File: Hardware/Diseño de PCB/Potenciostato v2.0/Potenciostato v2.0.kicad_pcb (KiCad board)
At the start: 2 copper layers, 82 x 100 mm, 129 parts, among them IC1 LMP7702MAX_NOPB, IC2 LMP7701MFX_NOPB, IC3 LMP7701MFX_NOPB, IC4 MAX5217GUA+, IC5 MAX4477ASA+, IC6 LM4040AIM3X-2.5_NOPB, IC7 LM4040A50IDBZR, IC8 OPA354AIDBVT, J1 Conn_Coaxial, J2 Conn_02x15_Odd_Even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

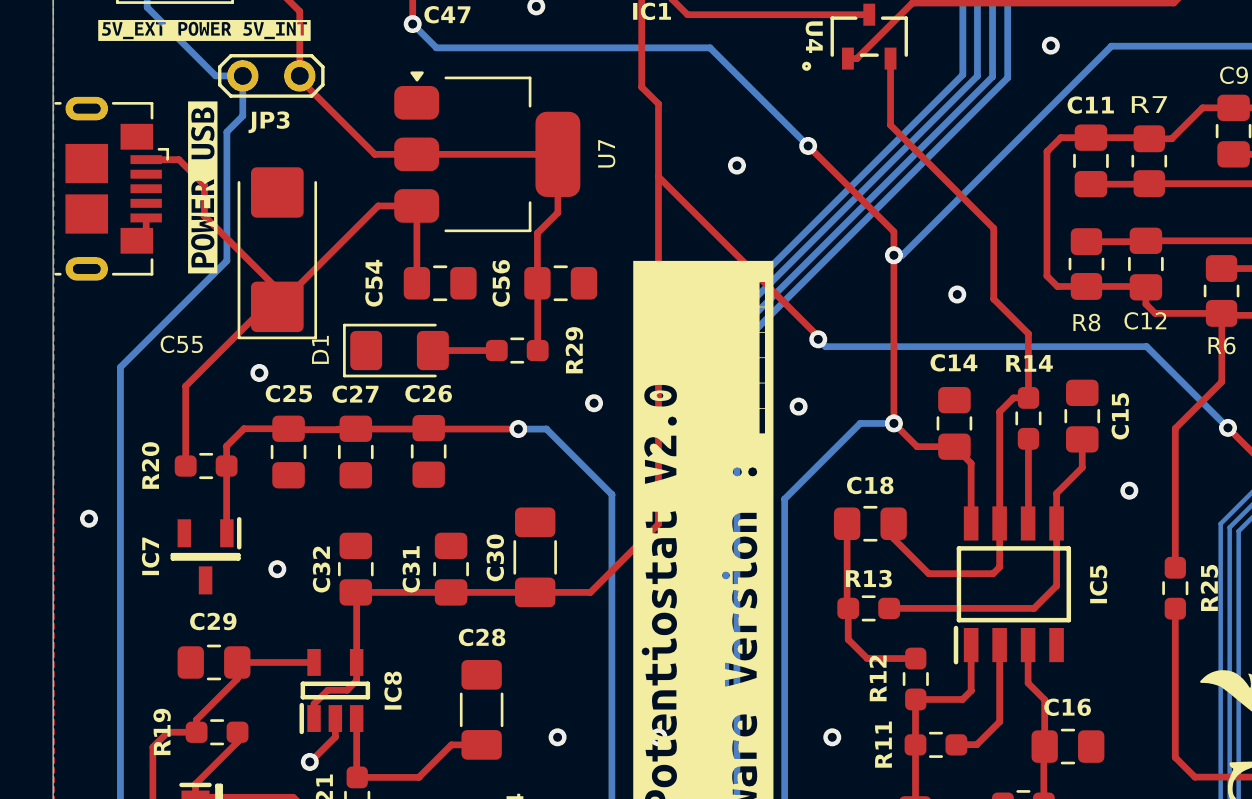
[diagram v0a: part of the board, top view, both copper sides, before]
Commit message: Hardware modifications. More notes added to the KiCad project related to hardware issues found during testing. USB Power and ground inverted corrected in design and PCB. MAX4477 replaced by OPA2320 in design and PCB. More notes with recommendations and advised can now be found in the schematics.
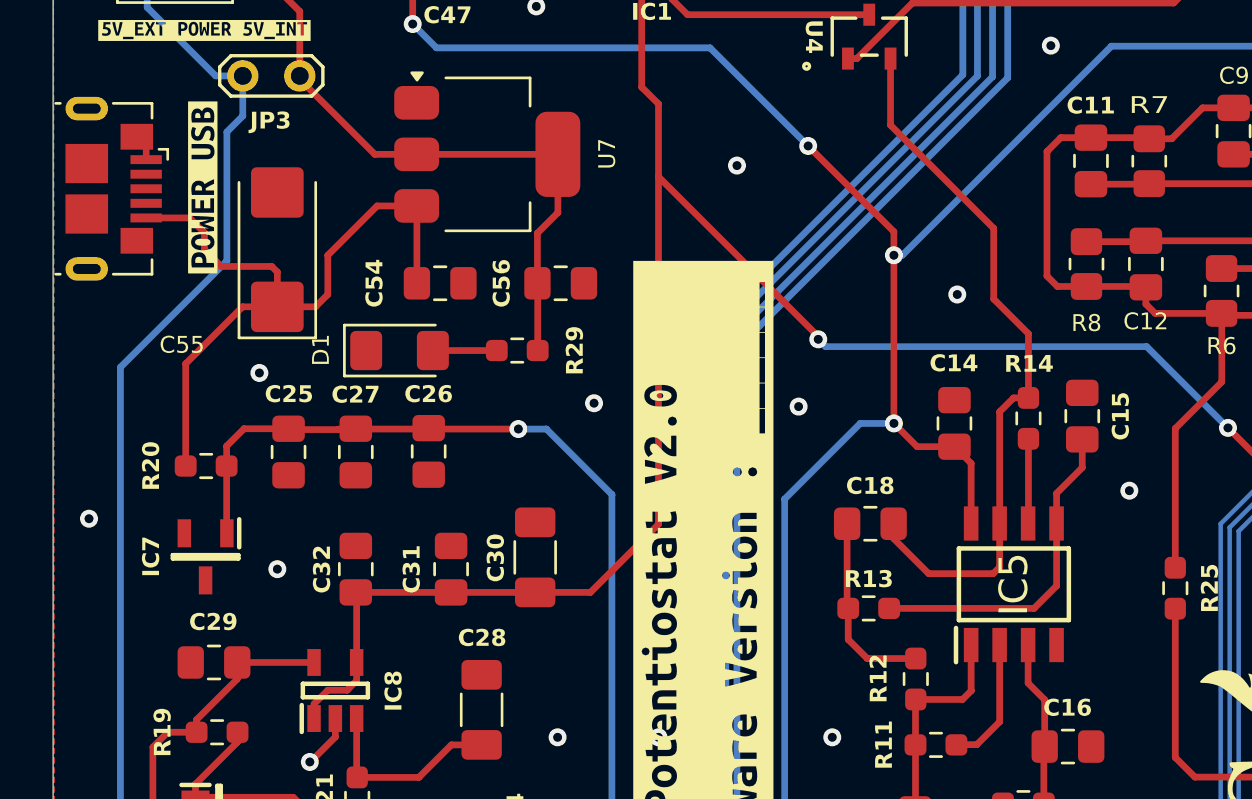
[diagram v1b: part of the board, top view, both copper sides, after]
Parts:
- C30: value 100u -> 10u
- C31: value 0.1u -> 1u
- C32: value 47u -> 0.1u
- IC5: value MAX4477ASA+ -> OPA2320AIDR; footprint potentiostat:SOIC127P600X175_MAX4477 -> potentiostat:SOIC127P600X175-8N
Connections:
- net /Etapa Amplificadora - Electrodos/X1 renamed /Amplifier Stage - Electrodes/X1
- net /Etapa Amplificadora - Electrodos/X2 renamed /Amplifier Stage - Electrodes/X2
- net /Etapa Amplificadora - Electrodos/X3 renamed /Amplifier Stage - Electrodes/X3
- net /Etapa Amplificadora - Electrodos/X4 renamed /Amplifier Stage - Electrodes/X4
- net /Etapa Amplificadora - Electrodos/X5 renamed /Amplifier Stage - Electrodes/X5
- net /Etapa Amplificadora - Electrodos/X6 renamed /Amplifier Stage - Electrodes/X6
- net /Etapa Amplificadora - Electrodos/X7 renamed /Amplifier Stage - Electrodes/X7
- C32 pad 1: GND -> +2V5
- C32 pad 2: +2V5 -> GND
- R16 pad 2: +3V3 -> +5V
- R17 pad 2: +3V3 -> +5V
- R18 pad 2: +3V3 -> +5V
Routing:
- net GND: track 22.5 -> 23.1 mm

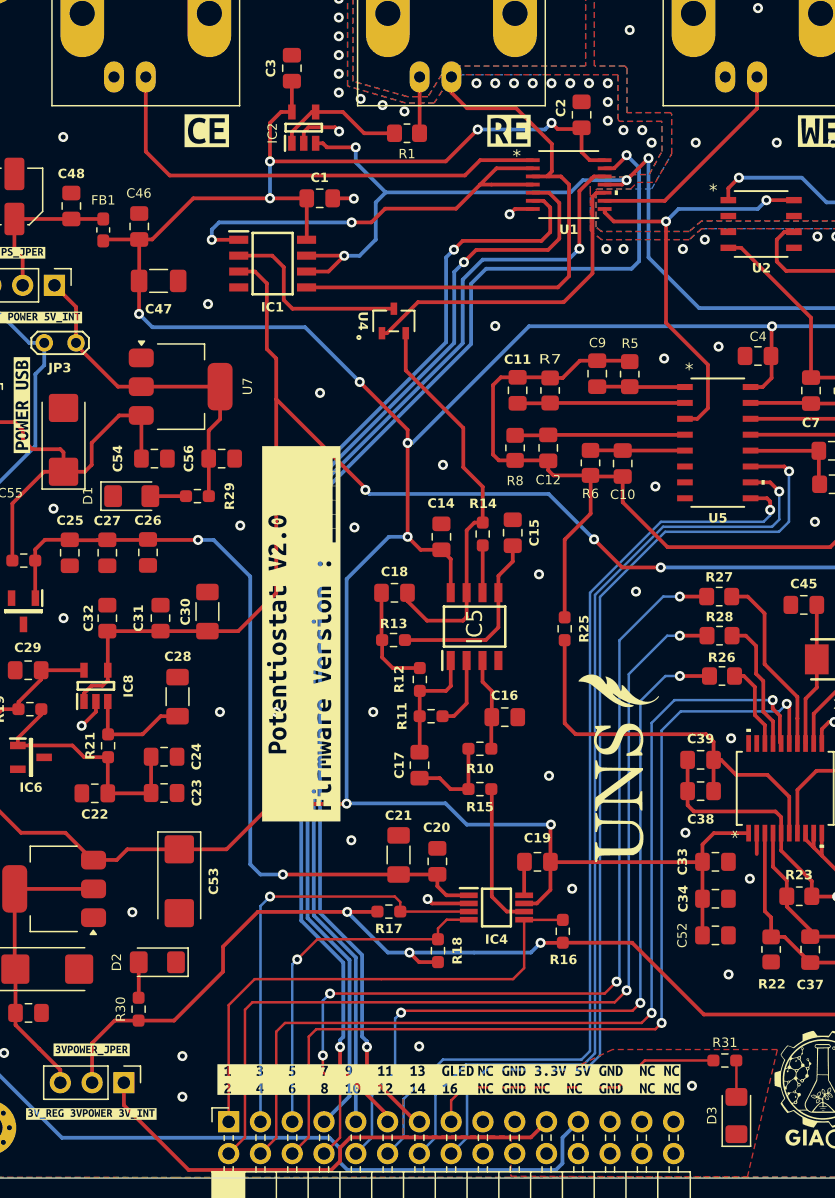
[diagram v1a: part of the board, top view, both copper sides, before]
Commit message: Hardware: Hardware Corrections in Potentiostat, small but important ones (WE electrode, Normal Open connection for electric disconnection in schematic and PCB. DAC I2C pull up resistors connected to 5V PCB layout corrected.). New project for ESP32 board: board design to hold ESP32 and LevelShifter for I2C3.3V to 5V. No more. No big changes in firmware and software, nothing to note, really small corrections in that were in the way.
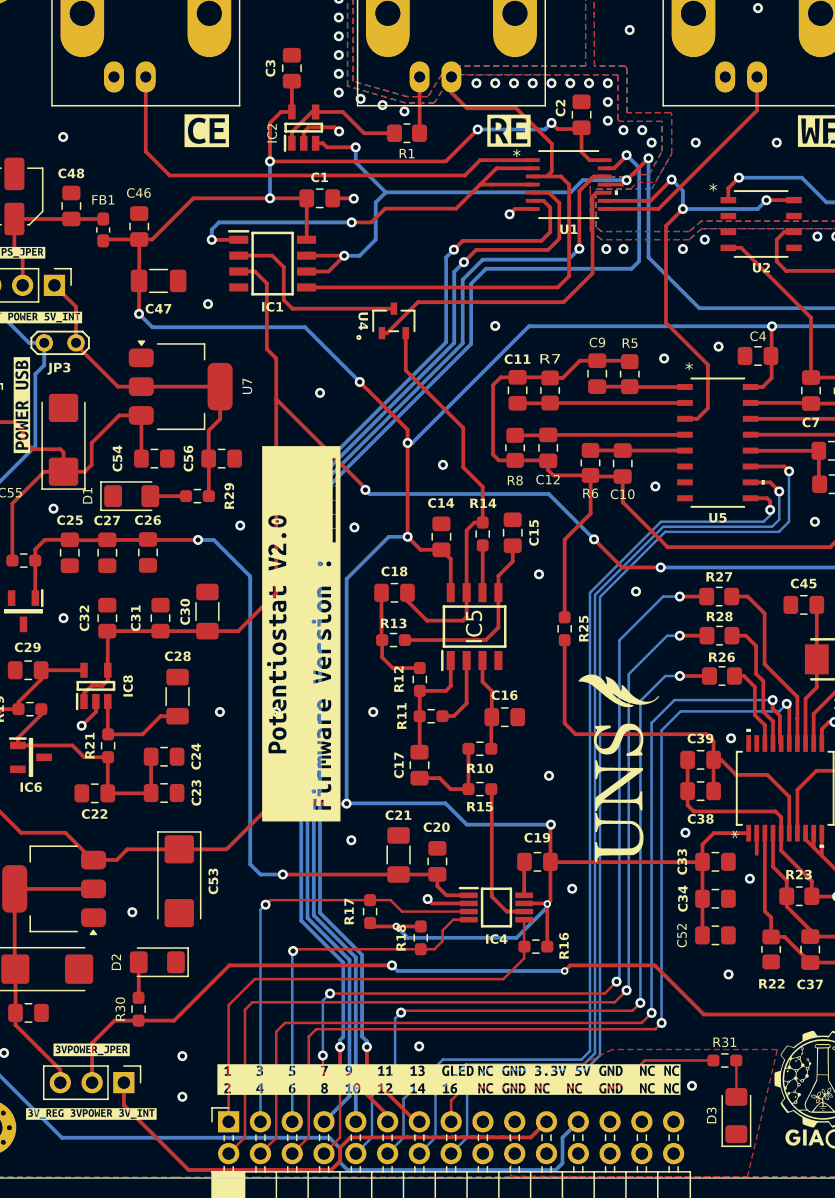
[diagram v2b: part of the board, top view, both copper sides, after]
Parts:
- moved R16 2.47 mm to (152.8, 136.5), turned to 0 degrees
- moved R18 1.72 mm to (143.6, 135.8), turned to 90 degrees
- moved R17 1.50 mm to (139.5, 133.7), turned to -90 degrees
- turned C32 to 90 degrees
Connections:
- U1 pad 8: Net-(U1-NO3) -> /WE
- U1 pad 9: /WE -> Net-(U1-NO3)
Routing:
- net +5V: track 300.9 -> 322.8 mm, vias 12 -> 14
- net +3V3: track 106.4 -> 96.4 mm, vias 3 -> 2
- net /DAC_NAUX: track 41.1 -> 37.6 mm
- net Net-(U1-NO3): track 34.9 -> 38.0 mm, vias 2 -> 3
- net /DAC_SCL: track 35.1 -> 34.3 mm
